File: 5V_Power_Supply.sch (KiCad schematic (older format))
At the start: 37 parts

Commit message: power supply overhaul
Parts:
- removed C?: NU, symbol Device:CP_Small
- C18, C19, C20, C21, C23: renamed from C?; footprint (none) -> Capacitor_SMD:C_1210_3225Metric_Pad1.42x2.65mm_HandSolder; Description (none) -> 100V MLCC 10%; Manufacturer_Part_Number (none) -> GRM32ER72A225KA35L; category (none) -> 5VREG; package (none) -> 1210
- C22: renamed from C?; footprint (none) -> Capacitor_SMD:C_0603_1608Metric_Pad1.05x0.95mm_HandSolder; Description (none) -> 100V MLCC 5%; Manufacturer_Part_Number (none) -> GRM1885C2A271JA01D; category (none) -> 5VREG; package (none) -> 0603
- C24, C27: renamed from C?; footprint (none) -> Capacitor_SMD:C_0603_1608Metric_Pad1.05x0.95mm_HandSolder; Description (none) -> 100V MLCC 10%; Manufacturer_Part_Number (none) -> GRM188R72A223KAC4D; category (none) -> 5VREG; package (none) -> 0603
- C25: renamed from C?; footprint (none) -> Capacitor_SMD:C_0603_1608Metric_Pad1.05x0.95mm_HandSolder; Description (none) -> 0603 UNPOPULATED; Manufacturer_Part_Number (none) -> N/A; category (none) -> 5VREG; package (none) -> 0603
- C26, C31: renamed from C?; footprint (none) -> Capacitor_SMD:C_0603_1608Metric_Pad1.05x0.95mm_HandSolder; Description (none) -> 100V MLCC 1%; Manufacturer_Part_Number (none) -> 06031A101FAT2A; category (none) -> 5VREG; package (none) -> 0603
- C28, C36: renamed from C?; footprint (none) -> Capacitor_SMD:C_0805_2012Metric_Pad1.15x1.40mm_HandSolder; Description (none) -> 100V MLCC 10%; Manufacturer_Part_Number (none) -> C2012X7R2A104K125AA; category (none) -> 5VREG; package (none) -> 0805
- C29: renamed from C?; footprint (none) -> Capacitor_SMD:C_0603_1608Metric_Pad1.05x0.95mm_HandSolder; Description (none) -> 16V MLCC 10%; Manufacturer_Part_Number (none) -> GCM188R71C105KA64J; category (none) -> VREG; package (none) -> 0603
- C30: renamed from C?; footprint (none) -> Capacitor_SMD:C_0603_1608Metric_Pad1.05x0.95mm_HandSolder; Description (none) -> 100V MLCC 10%; Manufacturer_Part_Number (none) -> GRM188R72A104KA35D; category (none) -> 5VREG; package (none) -> 0603
- C32: renamed from C?; footprint (none) -> Capacitor_SMD:C_0402_1005Metric; Description (none) -> 50V MLCC 10%; Manufacturer_Part_Number (none) -> GRM155R71H153KA12D; category (none) -> 5VREG; package (none) -> 0402
- C33: renamed from C?; footprint (none) -> Capacitor_SMD:C_0805_2012Metric_Pad1.15x1.40mm_HandSolder; Description (none) -> 100V MLCC 5%; Manufacturer_Part_Number (none) -> GRM2195C2A102JA01D; category (none) -> 5VREG; package (none) -> 0805
- C34, C35: renamed from C?; footprint (none) -> Capacitor_SMD:C_1210_3225Metric_Pad1.42x2.65mm_HandSolder; Description (none) -> 16V MLCC 10%; Manufacturer_Part_Number (none) -> GRM32ER61C476KE15L; category (none) -> 5VREG; package (none) -> 1210
- CP4: renamed from C?; footprint (none) -> Capacitor_SMD:CP_Elec_10x10.5; Description (none) -> 6.3V SMD Electrolytic 20%; Manufacturer_Part_Number (none) -> APXH6R3ARA471MJ80G; category (none) -> 5VREG
- D7: renamed from D?; value D_Small -> NU; footprint (none) -> Diode_SMD:D_SOD-128; Description (none) -> SOD-128 UNPOPULATED; category (none) -> 5VREG; package (none) -> SOD-128-2
- D8: renamed from D?; footprint (none) -> Package_TO_SOT_SMD:TO-263-2; Description (none) -> 15A 45V Schottky Rectifier; Manufacturer_Part_Number (none) -> MBRB1545CTT4G; category (none) -> 5VREG; package (none) -> D2PAK
- L1: renamed from L?; footprint (none) -> Inductor_SMD:L_12x12mm_H8mm; Description (none) -> 15A Fixed Inductor; Manufacturer_Part_Number (none) -> HC9-6R8-R; category (none) -> 5VREG
- Q4: renamed from Q?; footprint (none) -> Package_TO_SOT_SMD:TO-263-2; Description (none) -> PowerPak SO-8 NMOS 40V 10A; Manufacturer_Part_Number (none) -> SQM120N04-1M7L_GE3; category (none) -> 5VREG; package (none) -> PowerPak SO-8 Single
- R24: renamed from R?; footprint (none) -> Resistor_SMD:R_0603_1608Metric_Pad1.05x0.95mm_HandSolder; Description (none) -> Not Populated; Manufacturer_Part_Number (none) -> N/A; category (none) -> 5VREG; package (none) -> 0603
- R25: renamed from R?; value 16.2k -> 2.36k; footprint (none) -> Resistor_SMD:R_0603_1608Metric_Pad1.05x0.95mm_HandSolder; Description (none) -> 100mW Resistor 1%; Manufacturer_Part_Number (none) -> ERJ-S03F2371V; category (none) -> 5VREG; package (none) -> 0603
- R26: renamed from R?; footprint (none) -> Resistor_SMD:R_0805_2012Metric_Pad1.15x1.40mm_HandSolder; Description (none) -> 125mW Resistor 1%; Manufacturer_Part_Number (none) -> CR0805-FX-5492ELF; category (none) -> 5VREG; package (none) -> 0805
- R27: renamed from R?; footprint (none) -> Resistor_SMD:R_0603_1608Metric_Pad1.05x0.95mm_HandSolder; Description (none) -> 100mW Resistor 1%; Manufacturer_Part_Number (none) -> RT0603FRE0724K9L; category (none) -> 5VREG; package (none) -> 0603
- R28: renamed from R?; footprint (none) -> RL3720WT-R010-F:RESC2037X70N; Description (none) -> 1W Wide Current Sense Resistor 1%; Manufacturer_Part_Number (none) -> RL3720WT-R010-F; category (none) -> 5VREG; package (none) -> 1508
- R29: renamed from R?; value 18.2k -> 18k; footprint (none) -> Resistor_SMD:R_0603_1608Metric_Pad1.05x0.95mm_HandSolder; Description (none) -> 100mW Resistor 1%; Manufacturer_Part_Number (none) -> RN73H1JTTD1802F100; category (none) -> 5VREG; package (none) -> 0603
- R30: renamed from R?; footprint (none) -> Resistor_SMD:R_2512_6332Metric_Pad1.52x3.35mm_HandSolder; Description (none) -> 1W Resistor 1%; Manufacturer_Part_Number (none) -> ERJ-1TRQF5R1U; category (none) -> 5VREG; package (none) -> 2512
- R31: renamed from R?; footprint (none) -> Resistor_SMD:R_0805_2012Metric_Pad1.15x1.40mm_HandSolder; Description (none) -> 125mW Resistor 1%; Manufacturer_Part_Number (none) -> SFR10EZPF10R0; category (none) -> 5VREG; package (none) -> 0805
- R32: renamed from R?; footprint (none) -> Resistor_SMD:R_0603_1608Metric_Pad1.05x0.95mm_HandSolder; Description (none) -> 100mW Resistor 1%; Manufacturer_Part_Number (none) -> ERJ-S03F5111V; category (none) -> 5VREG; package (none) -> 0603
- R33: renamed from R?; footprint (none) -> Resistor_SMD:R_0603_1608Metric_Pad1.05x0.95mm_HandSolder; Description (none) -> 100mW Resistor 1%; Manufacturer_Part_Number (none) -> CR0603-FX-1621ELF; category (none) -> 5VREG; package (none) -> 0603
- TP14: renamed from TP?; footprint (none) -> TestPoint:TestPoint_Pad_1.0x1.0mm
- U7: renamed from U?; Description (none) -> LM25088MH-2 Buck Converter; Manufacturer_Part_Number (none) -> LM25088MH-2; category (none) -> 5VREG; package (none) -> SOP65
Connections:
- wire segments 122 -> 120
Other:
- note added: ""kelvin-connection""
- note added: "populate R's only for LiPo operation ->"
- moved on the sheet: C22, C26, R24, R27, TP14

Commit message: final final sch
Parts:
- removed Q4: Q_NMOS_DGS, Package_TO_SOT_SMD:TO-263-2, symbol Device:Q_NMOS_DGS
- added Q4: Q_NMOS_SGD, CSD18511Q5AT:CSD18511Q5AT, symbol Device:Q_NMOS_SGD
- D8: footprint Package_TO_SOT_SMD:TO-263-2 -> PMEG045V150EPDZ:NEXPERIA_PMEG045V150EPDZ
- R32: Manufacturer_Part_Number ERJ-S03F5111V -> ERJ-3EKF5111V
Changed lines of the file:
@@
 Wire Wire Line
 	7100 3950 7100 4100
-Wire Wire Line
-	7100 4100 7200 4100
 Text HLabel 7650 4100 2    50   Input ~ 0
 GND
@@
 	6800 3450 6800 3550
 Connection ~ 6800 3550
-$Comp
-L Device:Q_NMOS_DGS Q4
-U 1 1 61C56924
-P 7250 3100
-F 0 "Q4" H 7454 3146 50  0000 L CNN
-F 1 "Q_NMOS_DGS" H 7454 3055 50  0000 L CNN
-F 2 "Package_TO_SOT_SMD:TO-263-2" H 7450 3200 50  0001 C CNN
-F 3 "~" H 7250 3100 50  0001 C CNN
-F 4 "PowerPak SO-8 NMOS 40V 10A" H 7250 3100 50  0001 C CNN "Description"
-F 5 "SQM120N04-1M7L_GE3" H 7250 3100 50  0001 C CNN "Manufacturer_Part_Number"
-F 6 "5VREG" H 7250 3100 50  0001 C CNN "category"
-F 7 "PowerPak SO-8 Single" H 7250 3100 50  0001 C CNN "package"
-	1    7250 3100
-	1    0    0    -1
-$EndComp
 Wire Wire Line
 	7050 3100 6450 3100
@@
 F 0 "D8" H 7318 3775 50  0000 L CNN
 F 1 "Diode_Schottky_Common_Cathode" H 7318 3718 50  0001 L CNN
-F 2 "Package_TO_SOT_SMD:TO-263-2" H 7250 3750 50  0001 C CNN
+F 2 "PMEG045V150EPDZ:NEXPERIA_PMEG045V150EPDZ" H 7250 3750 50  0001 C CNN
 F 3 "~" H 7250 3750 50  0001 C CNN
 F 4 "15A 45V Schottky Rectifier" H 7200 3750 50  0001 C CNN "Description"
@@
 F 3 "~" H 10400 4450 50  0001 C CNN
 F 4 "100mW Resistor 1%" H 10400 4450 50  0001 C CNN "Description"
-F 5 "ERJ-S03F5111V" H 10400 4450 50  0001 C CNN "Manufacturer_Part_Number"
+F 5 "ERJ-3EKF5111V" H 10400 4450 50  0001 C CNN "Manufacturer_Part_Number"
 F 6 "5VREG" H 10400 4450 50  0001 C CNN "category"
 F 7 "0603" H 10400 4450 50  0001 C CNN "package"
@@
 Wire Wire Line
 	8650 3750 9450 3750
+Wire Wire Line
+	7100 4100 7200 4100
+$Comp
+L Device:Q_NMOS_SGD Q4
+U 1 1 61C1CCB6
+P 7250 3100
+F 0 "Q4" H 7454 3146 50  0000 L CNN
+F 1 "Q_NMOS_SGD" H 7454 3055 50  0000 L CNN
+F 2 "CSD18511Q5AT:CSD18511Q5AT" H 7450 3200 50  0001 C CNN
+F 3 "~" H 7250 3100 50  0001 C CNN
+	1    7250 3100
+	1    0    0    -1
+$EndComp
 $EndSCHEMATC

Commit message: [pcb] added copper planes
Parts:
- L1: footprint Inductor_SMD:L_12x12mm_H8mm -> SRP6060FA:L_6.3x6.3_H3
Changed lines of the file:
@@
 F 0 "L1" V 8535 3550 50  0000 C CNN
 F 1 "6.8uH" V 8444 3550 50  0000 C CNN
-F 2 "Inductor_SMD:L_12x12mm_H8mm" H 8350 3550 50  0001 C CNN
+F 2 "SRP6060FA:L_6.3x6.3_H3" H 8350 3550 50  0001 C CNN
 F 3 "~" H 8350 3550 50  0001 C CNN
 F 4 "15A Fixed Inductor" H 8350 3550 50  0001 C CNN "Description"

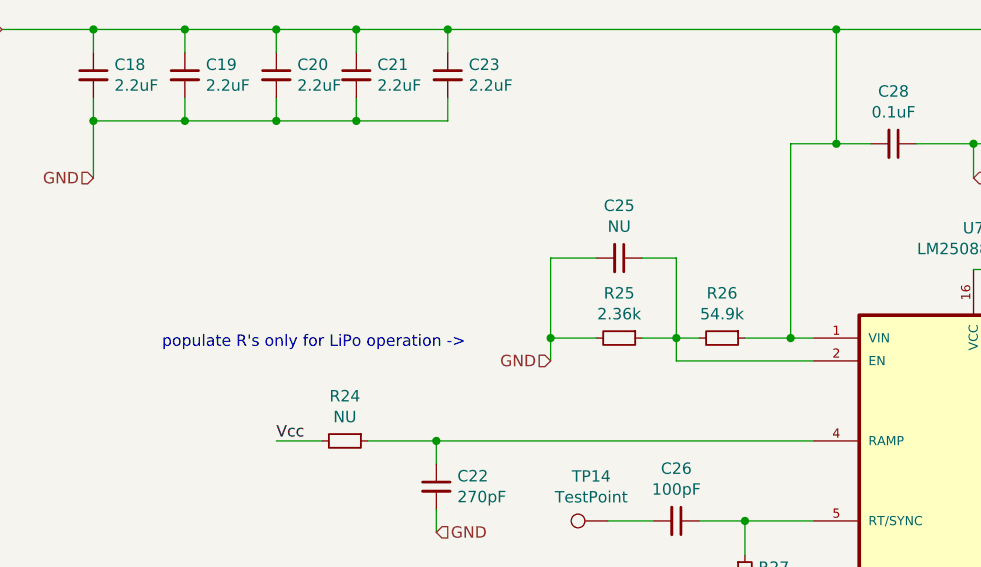
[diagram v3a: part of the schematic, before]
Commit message: [rev.2 fixes]  - fix Q4 net pin assignment  - removed UVLO  - fix kelvin connection on R_sense  - fix MCP2515 symbol + pinout  - changed oscillator capacitors for 18uF load capacitance  - PCA9615 biasing resistors
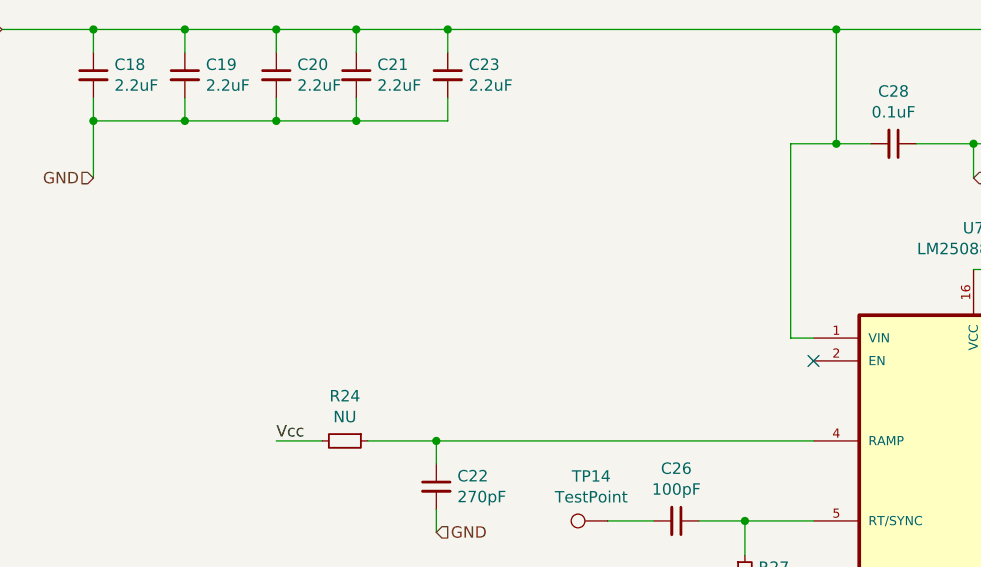
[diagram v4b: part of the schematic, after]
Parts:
- removed C25: NU, Capacitor_SMD:C_0603_1608Metric_Pad1.05x0.95mm_HandSolder, symbol Device:C_Small
- removed R25: 2.36k, Resistor_SMD:R_0603_1608Metric_Pad1.05x0.95mm_HandSolder, symbol Device:R_Small
- removed R26: 54.9k, Resistor_SMD:R_0805_2012Metric_Pad1.15x1.40mm_HandSolder, symbol Device:R_Small
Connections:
- no-connect marks 0 -> 1
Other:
- note removed: "populate R's only for LiPo operation ->"
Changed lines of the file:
@@
 Wire Wire Line
 	2700 3550 2900 3550
-$Comp
-L Device:R_Small R26
-U 1 1 61CD9D7E
-P 4650 3100
-F 0 "R26" V 4454 3100 50  0000 C CNN
-F 1 "54.9k" V 4545 3100 50  0000 C CNN
-F 2 "Resistor_SMD:R_0805_2012Metric_Pad1.15x1.40mm_HandSolder" H 4650 3100 50  0001 C CNN
-F 3 "~" H 4650 3100 50  0001 C CNN
-F 4 "125mW Resistor 1%" H 4650 3100 50  0001 C CNN "Description"
-F 5 "CR0805-FX-5492ELF" H 4650 3100 50  0001 C CNN "Manufacturer_Part_Number"
-F 6 "5VREG" H 4650 3100 50  0001 C CNN "category"
-F 7 "0805" H 4650 3100 50  0001 C CNN "package"
-	1    4650 3100
-	0    1    1    0
-$EndComp
-Wire Wire Line
-	5050 3200 4450 3200
 Wire Wire Line
 	5050 3100 4950 3100
-Wire Wire Line
-	4450 3200 4450 3100
-Wire Wire Line
-	4450 3100 4550 3100
-$Comp
-L Device:R_Small R25
-U 1 1 61CE3826
-P 4200 3100
-F 0 "R25" V 4004 3100 50  0000 C CNN
-F 1 "2.36k" V 4095 3100 50  0000 C CNN
-F 2 "Resistor_SMD:R_0603_1608Metric_Pad1.05x0.95mm_HandSolder" H 4200 3100 50  0001 C CNN
-F 3 "~" H 4200 3100 50  0001 C CNN
-F 4 "100mW Resistor 1%" H 4200 3100 50  0001 C CNN "Description"
-F 5 "ERJ-S03F2371V" H 4200 3100 50  0001 C CNN "Manufacturer_Part_Number"
-F 6 "5VREG" H 4200 3100 50  0001 C CNN "category"
-F 7 "0603" H 4200 3100 50  0001 C CNN "package"
-	1    4200 3100
-	0    1    1    0
-$EndComp
-Wire Wire Line
-	4300 3100 4450 3100
-Connection ~ 4450 3100
-Wire Wire Line
-	4450 3100 4450 2750
-$Comp
-L Device:C_Small C25
-U 1 1 61CE7B95
-P 4200 2750
-F 0 "C25" V 3971 2750 50  0000 C CNN
-F 1 "NU" V 4062 2750 50  0000 C CNN
-F 2 "Capacitor_SMD:C_0603_1608Metric_Pad1.05x0.95mm_HandSolder" H 4200 2750 50  0001 C CNN
-F 3 "~" H 4200 2750 50  0001 C CNN
-F 4 "0603 UNPOPULATED" H 4200 2750 50  0001 C CNN "Description"
-F 5 "N/A" H 4200 2750 50  0001 C CNN "Manufacturer_Part_Number"
-F 6 "5VREG" H 4200 2750 50  0001 C CNN "category"
-F 7 "0603" H 4200 2750 50  0001 C CNN "package"
-	1    4200 2750
-	0    1    1    0
-$EndComp
-Wire Wire Line
-	4300 2750 4450 2750
-Wire Wire Line
-	4100 2750 3900 2750
-Wire Wire Line
-	3900 2750 3900 3100
-Wire Wire Line
-	4100 3100 3900 3100
-Connection ~ 3900 3100
-Wire Wire Line
-	3900 3100 3900 3200
-Text HLabel 3900 3200 0    50   Input ~ 0
-GND
 $Comp
 L Device:C_Small C28
@@
 Wire Wire Line
 	4950 2250 4950 3100
-Connection ~ 4950 3100
-Wire Wire Line
-	4950 3100 4750 3100
 Wire Wire Line
 	5150 2250 5150 1750
@@
 Text Notes 7100 4200 0    50   ~ 0
 "kelvin-connection"
-Text Notes 2200 3150 0    50   ~ 0
-populate R's only for LiPo operation ->
 Wire Wire Line
 	5050 3900 4750 3900
@@
 	1    0    0    -1
 $EndComp
+NoConn ~ 5050 3200
 $EndSCHEMATC
